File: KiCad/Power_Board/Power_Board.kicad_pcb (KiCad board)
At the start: 4 copper layers, 101.6 x 63.5 mm, 13 parts, among them P1 CONN_LEFT_TOP, P2 CONN_RIGHT_TOP, P3 CONN_LEFT_BOTTOM, P4 CONN_RIGHT_BOTTOM

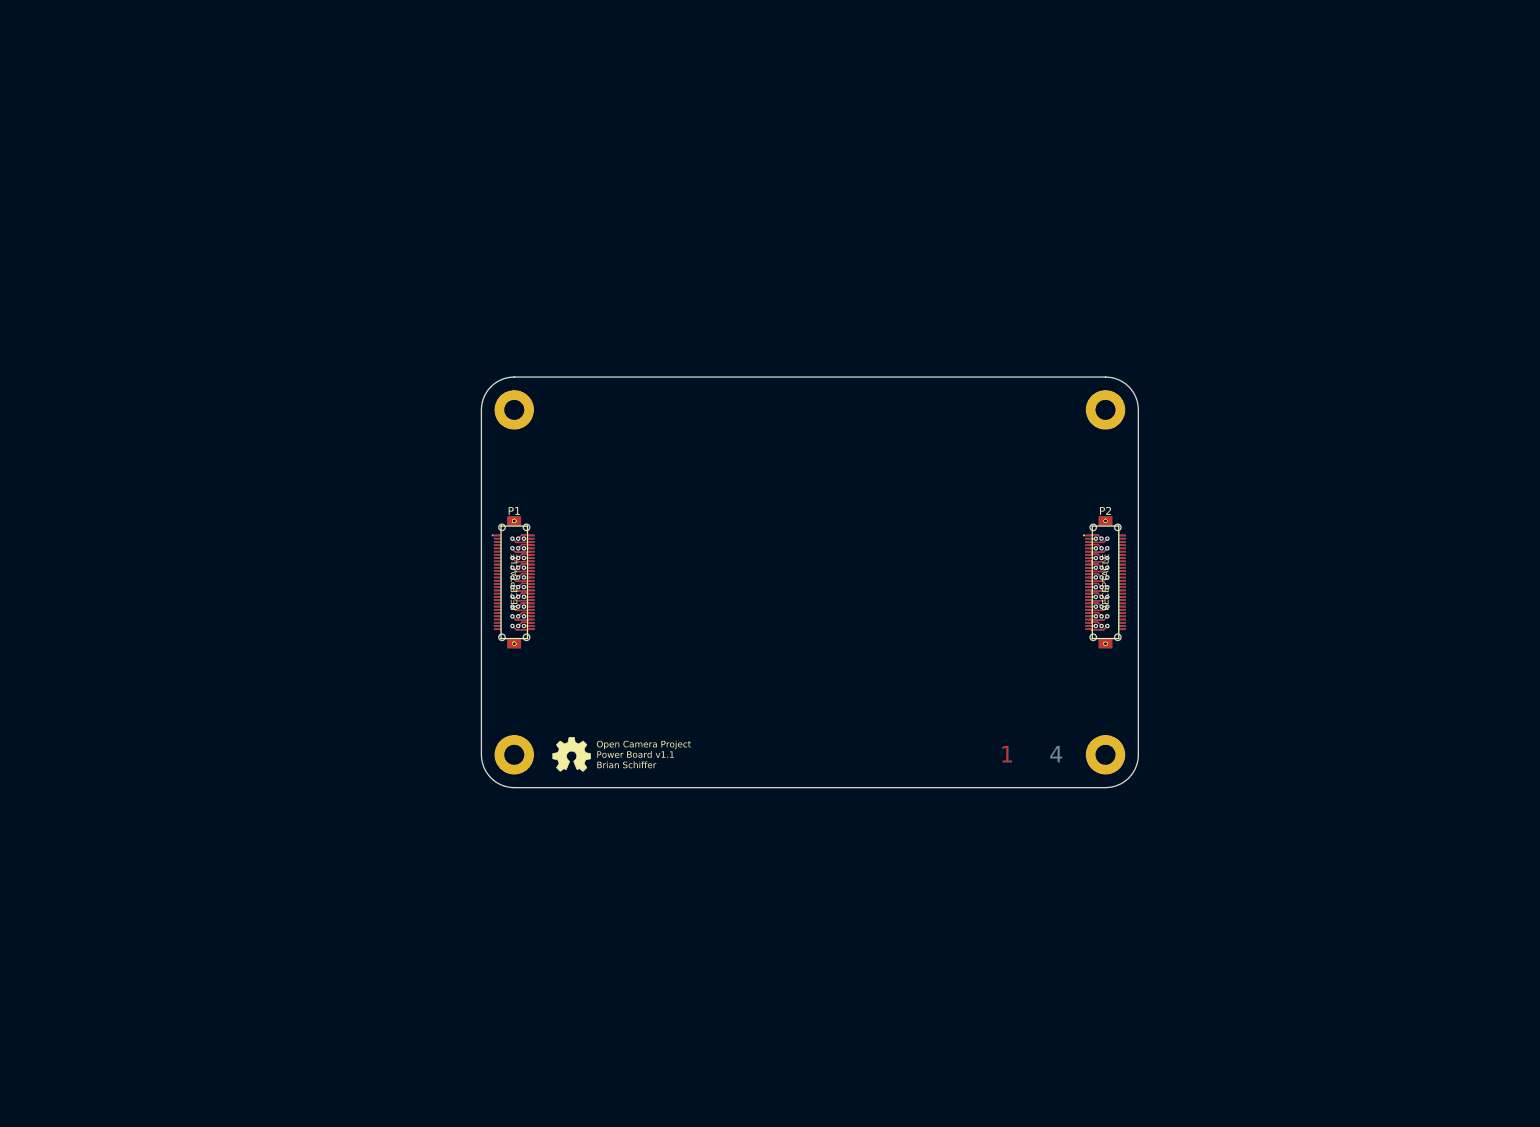
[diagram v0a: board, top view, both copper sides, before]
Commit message: Linked footprints to schematic.
Also cleaned up some footprint errors:
Changed IC footprint names to be invisible on the silkscreen layer.
Fixed test points that were lacking pin numbers causing netlist
failures.
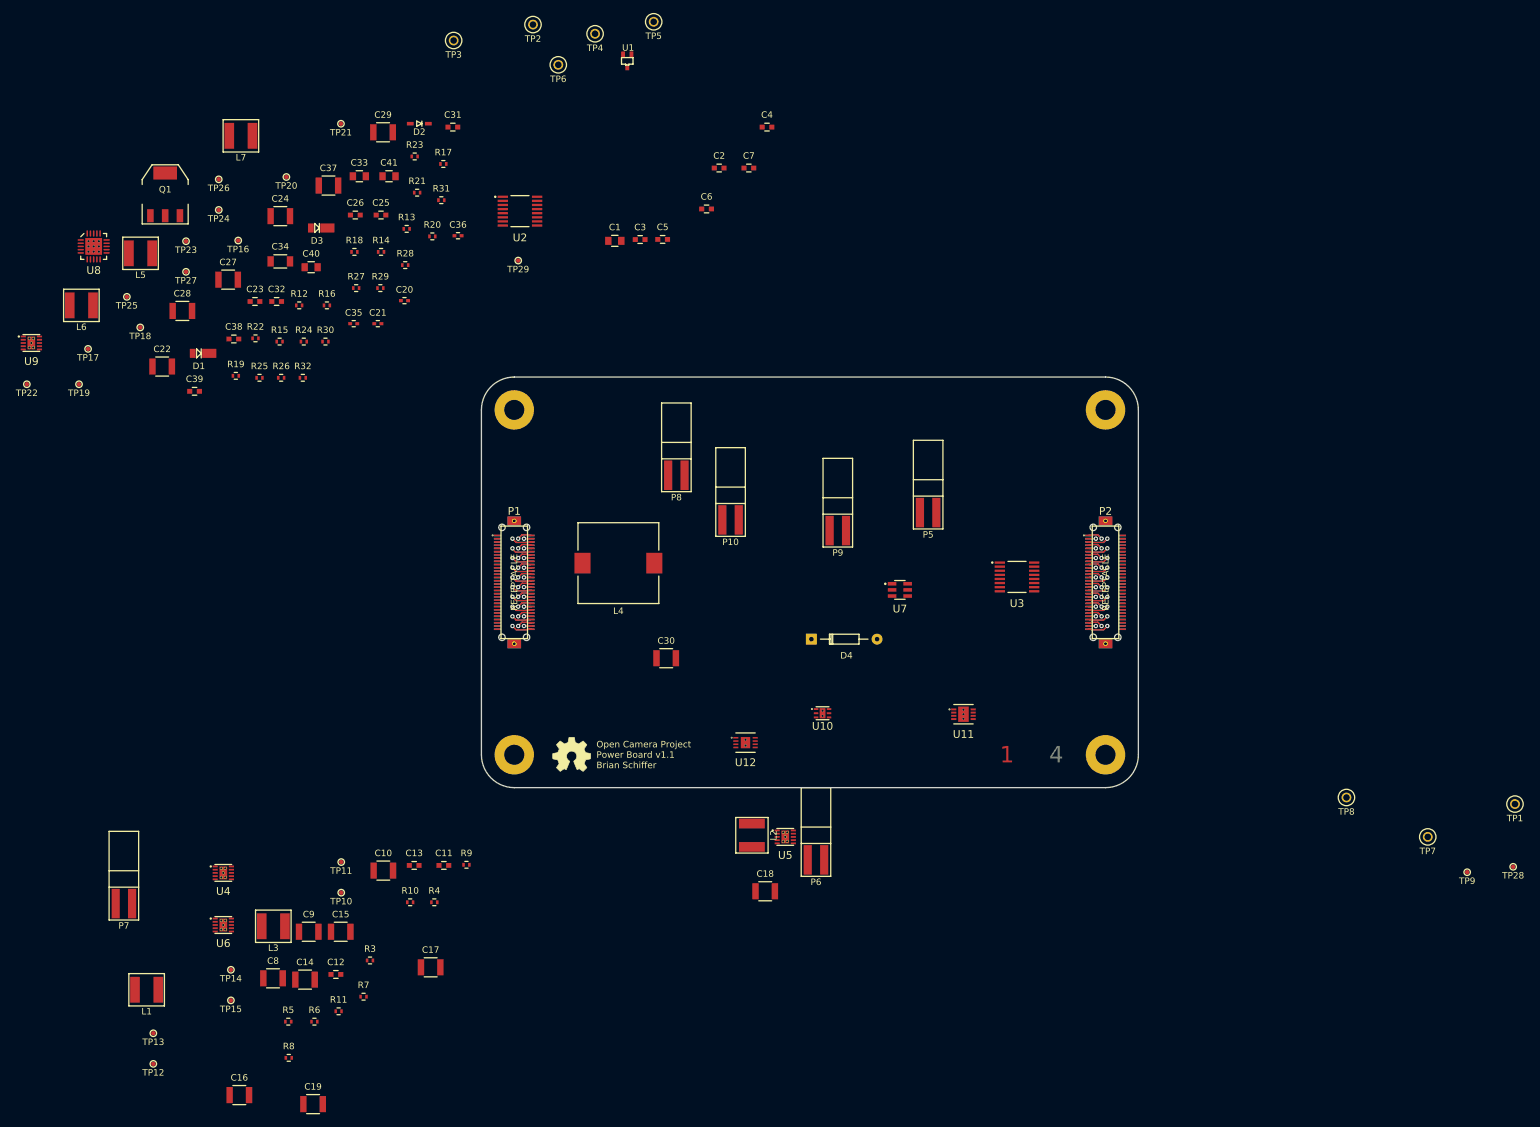
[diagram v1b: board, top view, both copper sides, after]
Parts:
- added C1: 4.7uF, Capacitors_SMD:C_0805, F.Cu at (109.5, 55.1)
- added C10: 10uF, Capacitors_SMD:C_1210, F.Cu at (73.7, 152.5)
- added C11: 0.1uF, Capacitors_SMD:C_0603, F.Cu at (83.1, 151.7)
- added C12: 0.1uF, Capacitors_SMD:C_0603, F.Cu at (66.4, 168.6)
- added C13: 0.1uF, Capacitors_SMD:C_0603, F.Cu at (78.5, 151.7)
- added C14: 10uF, Capacitors_SMD:C_1210, F.Cu at (61.6, 169.4)
- added C15: 10uF, Capacitors_SMD:C_1210, F.Cu at (67.1, 162.0)
- added C16: 10uF, Capacitors_SMD:C_1210, F.Cu at (51.5, 187.2)
- added C17: 10uF, Capacitors_SMD:C_1210, F.Cu at (81.1, 167.5)
- added C18: 10uF, Capacitors_SMD:C_1210, F.Cu at (132.8, 155.7)
- added C19: 10uF, Capacitors_SMD:C_1210, F.Cu at (62.9, 188.6)
- added C2: 0.1uF, Capacitors_SMD:C_0603, F.Cu at (125.7, 43.9)
- added C20: 47nF, Capacitors_SMD:C_0402, F.Cu at (77.0, 64.4)
- added C21: 47nF, Capacitors_SMD:C_0402, F.Cu at (72.9, 67.9)
- added C22: 10uF, Capacitors_SMD:C_1210, F.Cu at (39.5, 74.6)
- added C23: 1uF, Capacitors_SMD:C_0603, F.Cu at (53.9, 64.5)
- added C24: 10uF, Capacitors_SMD:C_1210, F.Cu at (57.8, 51.3)
- added C25: 0.1uF, Capacitors_SMD:C_0603, F.Cu at (73.4, 51.1)
- added C26: 1uF, Capacitors_SMD:C_0603, F.Cu at (69.4, 51.1)
- added C27: 10uF, Capacitors_SMD:C_1210, F.Cu at (49.7, 61.1)
- added C28: 10uF, Capacitors_SMD:C_1210, F.Cu at (42.6, 66.0)
- added C29: 10uF, Capacitors_SMD:C_1210, F.Cu at (73.7, 38.3)
- added C3: 1uF, Capacitors_SMD:C_0603, F.Cu at (113.4, 54.9)
- added C30: 10uF, Capacitors_SMD:C_1210, F.Cu at (117.5, 119.7)
- added C31: 20pF, Capacitors_SMD:C_0603, F.Cu at (84.5, 37.5)
- added C32: 1uF, Capacitors_SMD:C_0603, F.Cu at (57.2, 64.5)
- added C33: 2.2uF, Capacitors_SMD:C_0805, F.Cu at (70.0, 45.1)
- added C34: 1uF, Capacitors_SMD:C_1206, F.Cu at (57.8, 58.3)
- added C35: 1nF, Capacitors_SMD:C_0402, F.Cu at (69.1, 67.9)
- added C36: 1nF, Capacitors_SMD:C_0402, F.Cu at (85.3, 54.3)
- added C37: 10uF, Capacitors_SMD:C_1210, F.Cu at (65.2, 46.6)
- added C38: 1uF, Capacitors_SMD:C_0603, F.Cu at (50.6, 70.3)
- added C39: 100nF, Capacitors_SMD:C_0603, F.Cu at (44.5, 78.4)
- added C4: 1uF, Capacitors_SMD:C_0603, F.Cu at (133.1, 37.5)
- added C40: 2.2uF, Capacitors_SMD:C_0805, F.Cu at (62.6, 59.2)
- added C41: 2.2uF, Capacitors_SMD:C_0805, F.Cu at (74.6, 45.1)
- added C5: 1uF, Capacitors_SMD:C_0603, F.Cu at (116.9, 54.9)
- added C6: 0.1uF, Capacitors_SMD:C_0603, F.Cu at (123.7, 50.2)
- added C7: 0.1uF, Capacitors_SMD:C_0603, F.Cu at (130.3, 43.9)
- added C8: 10uF, Capacitors_SMD:C_1210, F.Cu at (56.7, 169.2)
- added C9: 10uF, Capacitors_SMD:C_1210, F.Cu at (62.2, 162.0)
- added D1: DFLS240, OpenCamera:DFLS240, F.Cu at (45.2, 72.5)
- added D2: 1N4148, OpenCamera:1N4148, F.Cu at (79.3, 37.0)
- added D3: DFLS240, OpenCamera:DFLS240, F.Cu at (63.5, 53.1)
- added D4: 1N5261, Diodes_ThroughHole:Diode_DO-35_SOD27_Horizontal_RM10, F.Cu at (139.9, 116.7)
- added L1: 3.3uH, OpenCamera:NRS5030, F.Cu at (37.1, 171.0)
- added L2: 3.3uH, OpenCamera:NRS5030, F.Cu at (130.7, 147.1)
- added L3: 3.3uH, OpenCamera:NRS5030, F.Cu at (56.7, 161.1)
- added L4: 47uH, OpenCamera:NS12555, F.Cu at (110.1, 105.0)
- added L5: 3.3uH, OpenCamera:NRS5030, F.Cu at (36.2, 57.1)
- added L6: 6.8uH, OpenCamera:NRS5030, F.Cu at (27.0, 65.1)
- added L7: 3.3uH, OpenCamera:NRS5030, F.Cu at (51.7, 38.9)
- added P10: CONN_02X01, OpenCamera:SMD_JUMPER, F.Cu at (127.4, 98.3)
- added P5: CONN_02X01, OpenCamera:SMD_JUMPER, F.Cu at (158.0, 97.2)
- added P6: CONN_02X01, OpenCamera:SMD_JUMPER, F.Cu at (140.6, 150.9)
- added P7: CONN_02X01, OpenCamera:SMD_JUMPER, F.Cu at (33.6, 157.6)
- added P8: CONN_02X01, OpenCamera:SMD_JUMPER, F.Cu at (119.0, 91.4)
- added P9: CONN_02X01, OpenCamera:SMD_JUMPER, F.Cu at (144.0, 99.9)
- added Q1: IRLL024NQ, SMD_Packages:SOT-223, F.Cu at (40.0, 47.9)
- added R10: 0, Resistors_SMD:R_0402, F.Cu at (77.9, 157.4)
- added R11: 0, Resistors_SMD:R_0402, F.Cu at (66.8, 174.3)
- added R12: 5.6k, Resistors_SMD:R_0402, F.Cu at (60.7, 65.1)
- added R13: 12k, Resistors_SMD:R_0402, F.Cu at (77.3, 53.3)
- added R14: 113k, Resistors_SMD:R_0402, F.Cu at (73.4, 56.8)
- added R15: 100k, Resistors_SMD:R_0402, F.Cu at (57.7, 70.7)
- added R16: 2.15M, Resistors_SMD:R_0402, F.Cu at (65.0, 65.1)
- added R17: 1.8M, Resistors_SMD:R_0402, F.Cu at (83.0, 43.2)
- added R18: 180k, Resistors_SMD:R_0402, F.Cu at (69.3, 56.8)
- added R19: 2.1M, Resistors_SMD:R_0402, F.Cu at (50.9, 76.0)
- added R20: 49.9k, Resistors_SMD:R_0402, F.Cu at (81.3, 54.4)
- added R21: 300k, Resistors_SMD:R_0402, F.Cu at (79.0, 47.7)
- added R22: 0, Resistors_SMD:R_0402, F.Cu at (54.0, 70.2)
- added R23: 0, Resistors_SMD:R_0402, F.Cu at (78.6, 42.1)
- added R24: 13k, Resistors_SMD:R_0402, F.Cu at (61.4, 70.7)
- added R25: 20k, Resistors_SMD:R_0402, F.Cu at (54.6, 76.3)
- added R26: 10k, Resistors_SMD:R_0402, F.Cu at (57.9, 76.3)
- added R27: 147k, Resistors_SMD:R_0402, F.Cu at (69.5, 62.4)
- added R28: 1k, Resistors_SMD:R_0402, F.Cu at (77.1, 58.9)
- added R29: 13k, Resistors_SMD:R_0402, F.Cu at (73.3, 62.4)
- added R3: 523k, Resistors_SMD:R_0402, F.Cu at (71.7, 166.4)
- added R30: 0, Resistors_SMD:R_0402, F.Cu at (64.8, 70.7)
- added R31: 0, Resistors_SMD:R_0402, F.Cu at (82.7, 48.8)
- added R32: 0, Resistors_SMD:R_0402, F.Cu at (61.3, 76.3)
- added R4: 200k, Resistors_SMD:R_0402, F.Cu at (81.6, 157.4)
- added R5: 1.8M, Resistors_SMD:R_0402, F.Cu at (59.0, 175.9)
- added R6: 200k, Resistors_SMD:R_0402, F.Cu at (63.1, 175.9)
- added R7: 1.2M, Resistors_SMD:R_0402, F.Cu at (70.7, 172.0)
- added R8: 210k, Resistors_SMD:R_0402, F.Cu at (59.1, 181.5)
- added R9: 0, Resistors_SMD:R_0402, F.Cu at (86.6, 151.6)
- added TP1: Test_Point, OpenCamera:TEST_CLIP, F.Cu at (248.7, 142.2)
- added TP10: Test_Point, OpenCamera:TEST_POINT_SMD, F.Cu at (67.2, 155.9)
- added TP11: Test_Point, OpenCamera:TEST_POINT_SMD, F.Cu at (67.2, 151.2)
- added TP12: Test_Point, OpenCamera:TEST_POINT_SMD, F.Cu at (38.2, 182.4)
- added TP13: Test_Point, OpenCamera:TEST_POINT_SMD, F.Cu at (38.2, 177.7)
- added TP14: Test_Point, OpenCamera:TEST_POINT_SMD, F.Cu at (50.2, 167.9)
- added TP15: Test_Point, OpenCamera:TEST_POINT_SMD, F.Cu at (50.2, 172.6)
- added TP16: Test_Point, OpenCamera:TEST_POINT_SMD, F.Cu at (51.3, 55.1)
- added TP17: Test_Point, OpenCamera:TEST_POINT_SMD, F.Cu at (28.1, 71.8)
- added TP18: Test_Point, OpenCamera:TEST_POINT_SMD, F.Cu at (36.1, 68.5)
- added TP19: Test_Point, OpenCamera:TEST_POINT_SMD, F.Cu at (26.7, 77.3)
- added TP2: Test_Point, OpenCamera:TEST_CLIP, F.Cu at (96.9, 21.7)
- added TP20: Test_Point, OpenCamera:TEST_POINT_SMD, F.Cu at (58.7, 45.3)
- added TP21: Test_Point, OpenCamera:TEST_POINT_SMD, F.Cu at (67.2, 37.0)
- added TP22: Test_Point, OpenCamera:TEST_POINT_SMD, F.Cu at (18.6, 77.3)
- added TP23: Test_Point, OpenCamera:TEST_POINT_SMD, F.Cu at (43.2, 55.2)
- added TP24: Test_Point, OpenCamera:TEST_POINT_SMD, F.Cu at (48.3, 50.4)
- added TP25: Test_Point, OpenCamera:TEST_POINT_SMD, F.Cu at (34.1, 63.8)
- added TP26: Test_Point, OpenCamera:TEST_POINT_SMD, F.Cu at (48.3, 45.6)
- added TP27: Test_Point, OpenCamera:TEST_POINT_SMD, F.Cu at (43.2, 59.9)
- added TP28: Test_Point, OpenCamera:TEST_POINT_SMD, F.Cu at (248.5, 151.9)
- added TP29: Test_Point, OpenCamera:TEST_POINT_SMD, F.Cu at (94.6, 58.2)
- added TP3: Test_Point, OpenCamera:TEST_CLIP, F.Cu at (84.6, 24.2)
- added TP4: Test_Point, OpenCamera:TEST_CLIP, F.Cu at (106.5, 23.1)
- added TP5: Test_Point, OpenCamera:TEST_CLIP, F.Cu at (115.5, 21.3)
- added TP6: Test_Point, OpenCamera:TEST_CLIP, F.Cu at (100.8, 27.9)
- added TP7: Test_Point, OpenCamera:TEST_CLIP, F.Cu at (235.3, 147.3)
- added TP8: Test_Point, OpenCamera:TEST_CLIP, F.Cu at (222.7, 141.2)
- added TP9: Test_Point, OpenCamera:TEST_POINT_SMD, F.Cu at (241.4, 152.8)
- added U1: AD1583, SMD_Packages:SOT-323, F.Cu at (111.5, 27.3)
- added U10: ADP7142_CSP, OpenCamera:ADP7142, F.Cu at (141.7, 128.2)
- added U11: ADP7182_CSP, OpenCamera:ADP7182, F.Cu at (163.4, 128.3)
- added U12: ADP3335_CSP, OpenCamera:ADP3335, F.Cu at (129.7, 132.7)
- added U2: MAX5259, OpenCamera:QSOP_16, F.Cu at (94.9, 50.5)
- added U3: MAX5259, OpenCamera:QSOP_16, F.Cu at (171.7, 107.1)
- added U4: TPS63030, OpenCamera:TPS63030, F.Cu at (49.0, 152.9)
- added U5: TPS63030, OpenCamera:TPS63030, F.Cu at (135.9, 147.3)
- added U6: TPS63030, OpenCamera:TPS63030, F.Cu at (49.0, 160.9)
- added U7: MAX152x, OpenCamera:SOT_623, F.Cu at (153.6, 109.1)
- added U8: ADP5070, OpenCamera:ADP5070, F.Cu at (28.9, 56.0)
- added U9: TPS63030, OpenCamera:TPS63030, F.Cu at (19.3, 70.9)
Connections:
- net /connectors/L2 renamed /Digital_Power/5V
- net /connectors/L3 renamed /Digital_Power/3.3V
- net /connectors/L4 renamed /Digital_Power/1.8V
- net /connectors/R1 renamed /Analog_Power/5Va
- net /connectors/R2 renamed /Analog_Power/15Va
- net /connectors/R3 renamed /Analog_Power/-15Va
- net /connectors/R4 renamed /Analog_Power/50Va
- P1 pad 1: GNDD -> GND
- P1 pad 11: GNDD -> GND
- P1 pad 13: GNDD -> GND
- P1 pad 15: GNDD -> GND
- P1 pad 17: GNDD -> GND
- P1 pad 19: GNDD -> GND
- P1 pad 21: GNDD -> GND
- P1 pad 23: GNDD -> GND
- P1 pad 25: GNDD -> GND
- P1 pad 27: GNDD -> GND
- P1 pad 29: GNDD -> GND
- P1 pad 3: GNDD -> GND
- P1 pad 31: GNDD -> GND
- P1 pad 33: GNDD -> GND
- P1 pad 35: GNDD -> GND
- P1 pad 37: GNDD -> GND
- P1 pad 39: GNDD -> GND
- P1 pad 41: GNDD -> GND
- P1 pad 43: GNDD -> GND
- P1 pad 45: GNDD -> GND
- P1 pad 47: GNDD -> GND
- P1 pad 49: GNDD -> GND
- P1 pad 5: GNDD -> GND
- P1 pad 51: GNDD -> GND
- P1 pad 53: GNDD -> GND
- P1 pad 55: GNDD -> GND
- P1 pad 57: GNDD -> GND
- P1 pad 59: GNDD -> GND
- P1 pad 61: GNDD -> GND
- P1 pad 62: GNDD -> GND
- P1 pad 7: GNDD -> GND
- P1 pad 9: GNDD -> GND
- P2 pad 10: GNDA -> GND
- P2 pad 12: GNDA -> GND
- P2 pad 14: GNDA -> GND
- P2 pad 16: GNDA -> GND
- P2 pad 18: GNDA -> GND
- P2 pad 2: GNDA -> GND
- P2 pad 20: GNDA -> GND
- P2 pad 22: GNDA -> GND
- P2 pad 24: GNDA -> GND
- P2 pad 26: GNDA -> GND
- P2 pad 28: GNDA -> GND
- P2 pad 30: GNDA -> GND
- P2 pad 32: GNDA -> GND
- P2 pad 34: GNDA -> GND
- P2 pad 36: GNDA -> GND
- P2 pad 38: GNDA -> GND
- P2 pad 4: GNDA -> GND
- P2 pad 40: GNDA -> GND
- P2 pad 42: GNDA -> GND
- P2 pad 44: GNDA -> GND
- P2 pad 46: GNDA -> GND
- P2 pad 48: GNDA -> GND
- P2 pad 50: GNDA -> GND
- P2 pad 52: GNDA -> GND
- P2 pad 54: GNDA -> GND
- P2 pad 56: GNDA -> GND
- P2 pad 58: GNDA -> GND
- P2 pad 6: GNDA -> GND
- P2 pad 60: GNDA -> GND
- P2 pad 61: GNDA -> GND
- P2 pad 62: GNDA -> GND
- P2 pad 8: GNDA -> GND
- P3 pad 10: GNDD -> GND
- P3 pad 12: GNDD -> GND
- P3 pad 14: GNDD -> GND
- P3 pad 16: GNDD -> GND
- P3 pad 18: GNDD -> GND
- P3 pad 2: GNDD -> GND
- P3 pad 20: GNDD -> GND
- P3 pad 22: GNDD -> GND
- P3 pad 24: GNDD -> GND
- P3 pad 26: GNDD -> GND
- P3 pad 28: GNDD -> GND
- P3 pad 30: GNDD -> GND
- P3 pad 32: GNDD -> GND
- P3 pad 34: GNDD -> GND
- P3 pad 36: GNDD -> GND
- P3 pad 38: GNDD -> GND
- P3 pad 4: GNDD -> GND
- P3 pad 40: GNDD -> GND
- P3 pad 42: GNDD -> GND
- P3 pad 44: GNDD -> GND
- P3 pad 46: GNDD -> GND
- P3 pad 48: GNDD -> GND
- P3 pad 50: GNDD -> GND
- P3 pad 52: GNDD -> GND
- P3 pad 54: GNDD -> GND
- P3 pad 56: GNDD -> GND
- P3 pad 58: GNDD -> GND
- P3 pad 6: GNDD -> GND
- P3 pad 60: GNDD -> GND
- P3 pad 61: GNDD -> GND
- P3 pad 62: GNDD -> GND
- P3 pad 8: GNDD -> GND
- P4 pad 1: GNDA -> GND
- P4 pad 11: GNDA -> GND
- P4 pad 13: GNDA -> GND
- P4 pad 15: GNDA -> GND
- P4 pad 17: GNDA -> GND
- P4 pad 19: GNDA -> GND
- P4 pad 21: GNDA -> GND
- P4 pad 23: GNDA -> GND
- P4 pad 25: GNDA -> GND
- P4 pad 27: GNDA -> GND
- P4 pad 29: GNDA -> GND
- P4 pad 3: GNDA -> GND
- P4 pad 31: GNDA -> GND
- P4 pad 33: GNDA -> GND
- P4 pad 35: GNDA -> GND
- P4 pad 37: GNDA -> GND
- P4 pad 39: GNDA -> GND
- P4 pad 41: GNDA -> GND
- P4 pad 43: GNDA -> GND
- P4 pad 45: GNDA -> GND
- P4 pad 47: GNDA -> GND
- P4 pad 49: GNDA -> GND
- P4 pad 5: GNDA -> GND
- P4 pad 51: GNDA -> GND
- P4 pad 53: GNDA -> GND
- P4 pad 55: GNDA -> GND
- P4 pad 57: GNDA -> GND
- P4 pad 59: GNDA -> GND
- P4 pad 61: GNDA -> GND
- P4 pad 62: GNDA -> GND
- P4 pad 7: GNDA -> GND
- P4 pad 9: GNDA -> GND

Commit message: Rough PCB component placement.
Organized parts by module and roughly placed them in appropriate
locations on the board.

Also fixed a couple of test points that weren't properly connected to a
net.
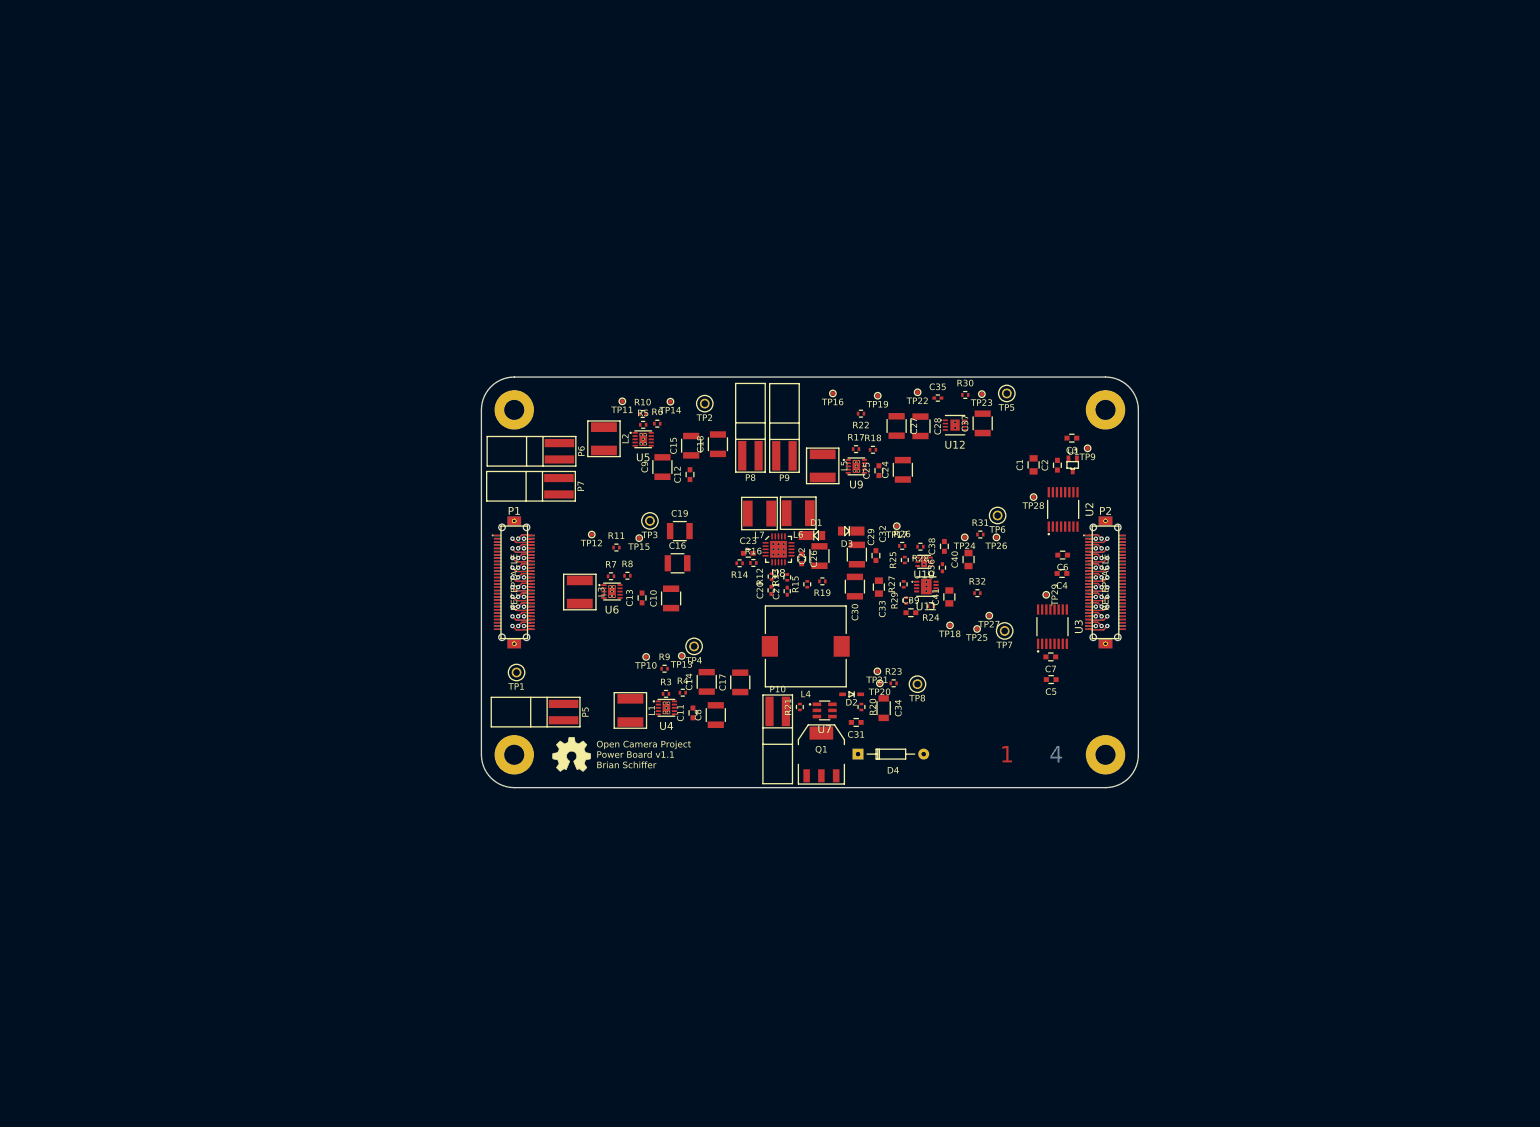
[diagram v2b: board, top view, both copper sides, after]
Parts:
- moved TP1 155.7 mm to (94.3, 121.9)
- moved TP25 141.2 mm to (165.6, 115.2)
- moved TP22 137.8 mm to (156.4, 78.6)
- moved TP27 135.1 mm to (167.4, 113.1)
- moved TP18 133.4 mm to (161.4, 114.6)
- moved Q1 133.4 mm to (141.5, 134.6)
- moved TP26 132.4 mm to (168.6, 101.0)
- moved U9 129.0 mm to (146.9, 90.0)
- moved TP17 128.0 mm to (153.1, 99.3)
- moved TP24 126.0 mm to (163.7, 101.0)
- moved TP23 125.3 mm to (166.3, 78.8)
- moved TP19 123.5 mm to (150.2, 79.1)
- moved TP20 120.6 mm to (150.5, 123.6)
- moved TP21 118.6 mm to (150.1, 121.7)
- moved C34 116.1 mm to (151.1, 127.4), turned to 270 degrees
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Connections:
- TP17 pad 1: Net-(TP17-Pad1) -> /Analog_Power/+16V
- TP18 pad 1: Net-(TP18-Pad1) -> /Analog_Power/-16V

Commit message: Connected GND & GNDA since this is the power board which supplies both.
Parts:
- moved TP1 12.6 mm to (106.9, 120.9)
- moved P5 3.31 mm to (100.7, 124.8)
- moved L2 0.42 mm to (108.3, 85.9)
- moved P6 0.25 mm to (100.7, 87.7)
- moved P7 0.18 mm to (100.7, 93.1)
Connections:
- net GND renamed GNDA
- U2 pad 11: /connectors/L5 -> /connectors/L8
- U2 pad 12: /connectors/L7 -> /connectors/L5
- U2 pad 13: /connectors/L8 -> /connectors/L6
- U3 pad 11: /connectors/L6 -> /connectors/L9
- U3 pad 12: /connectors/L7 -> /connectors/L5
- U3 pad 13: /connectors/L8 -> /connectors/L6
